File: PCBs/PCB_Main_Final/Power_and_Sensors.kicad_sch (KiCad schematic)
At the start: 26 parts, among them J10 fan connector, J7 XT60-M, J8 HUB75, J9 fan connector, Q2 Fan_NMOS, U10 AMS1117-3.3

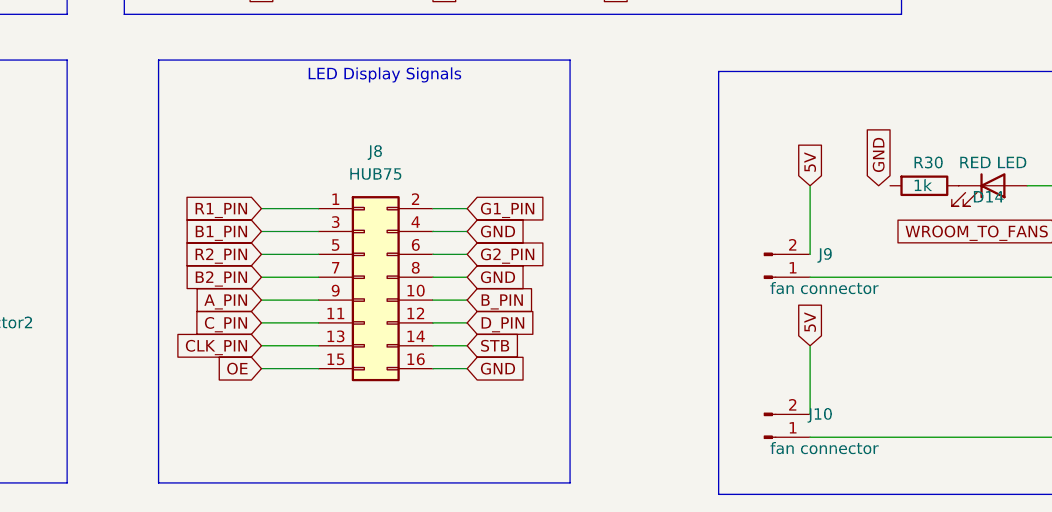
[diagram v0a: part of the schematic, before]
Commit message: finished Main and Light Sensor PCBs
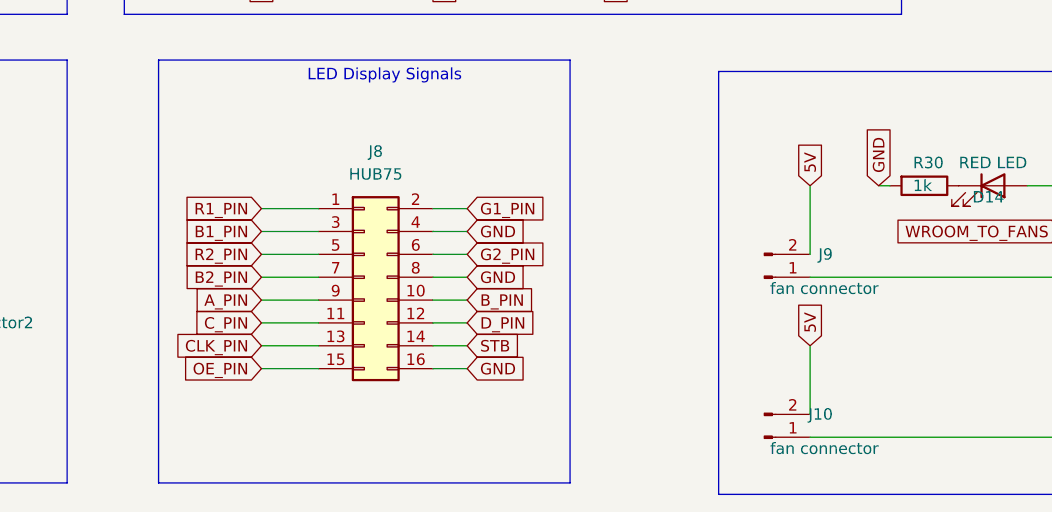
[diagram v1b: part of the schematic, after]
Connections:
- net GND: now also R30.2
- net OE renamed OE_PIN
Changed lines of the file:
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@@
+    (stroke (width 0) (type default))
+  )
+  (wire (pts (xy 156.21 85.09) (xy 157.48 85.09))
     (stroke (width 0) (type default))
   )
@@
     )
   )
-  (global_label "OE" (shape input) (at 87.63 105.41 180) (fields_autoplaced)
+  (global_label "OE_PIN" (shape input) (at 87.63 105.41 180) (fields_autoplaced)
     (effects (font (size 1.27 1.27)) (justify right))
-    (property "Intersheetrefs" "${INTERSHEET_REFS}" (at 82.1653 105.41 0)
+    (property "Intersheetrefs" "${INTERSHEET_REFS}" (at 77.9924 105.41 0)
       (effects (font (size 1.27 1.27)) (justify right) hide)
     )
